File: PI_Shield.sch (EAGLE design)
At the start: 66 parts, among them J10 T2I, J11 T2I, J12 T2I, J13 DF13-4P-1.25DSA, J14 DF13-4P-1.25DSA, J15 DF13-4P-1.25DSA, J16 T2I5P, Q1 220mA/50V/3.5Ω, Q3 220mA/50V/3.5Ω, Q4 220mA/50V/3.5Ω, Q5 2.5A/30V/105mΩ, U1 MAX1136EUA-T, U2 AZ1117EH-3.3TRG1, Y1 ECS-80-S-4X

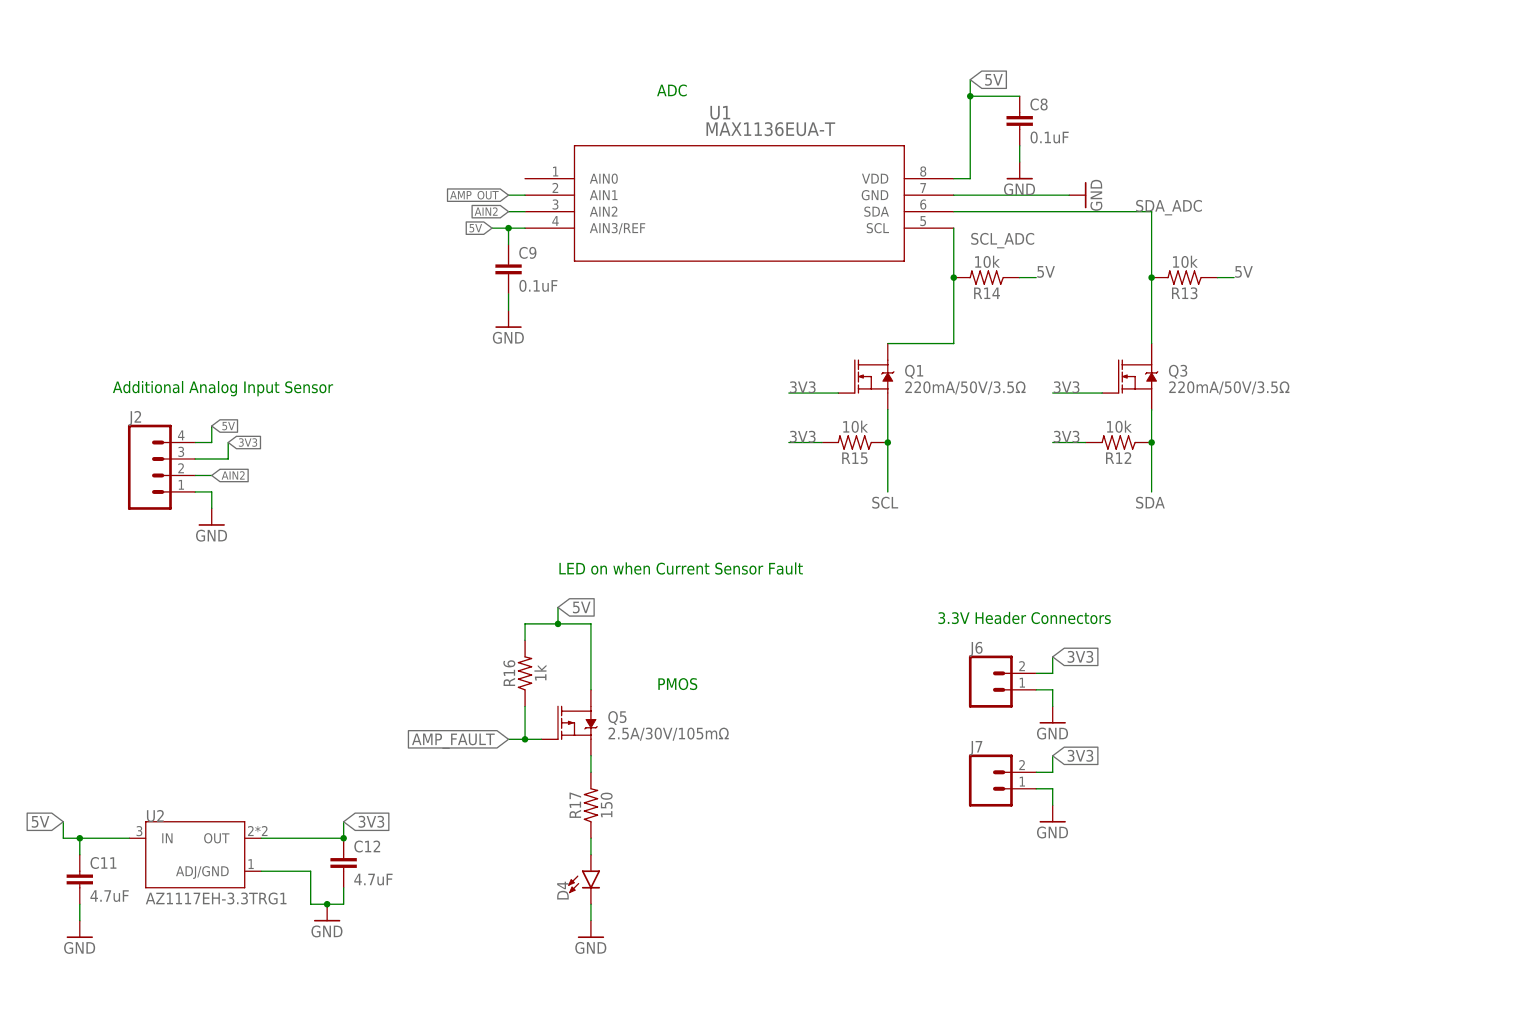
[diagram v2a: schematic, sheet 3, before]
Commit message: Added Pi 4 and Current Sensor; Routed Interrupt pins signals to Pi
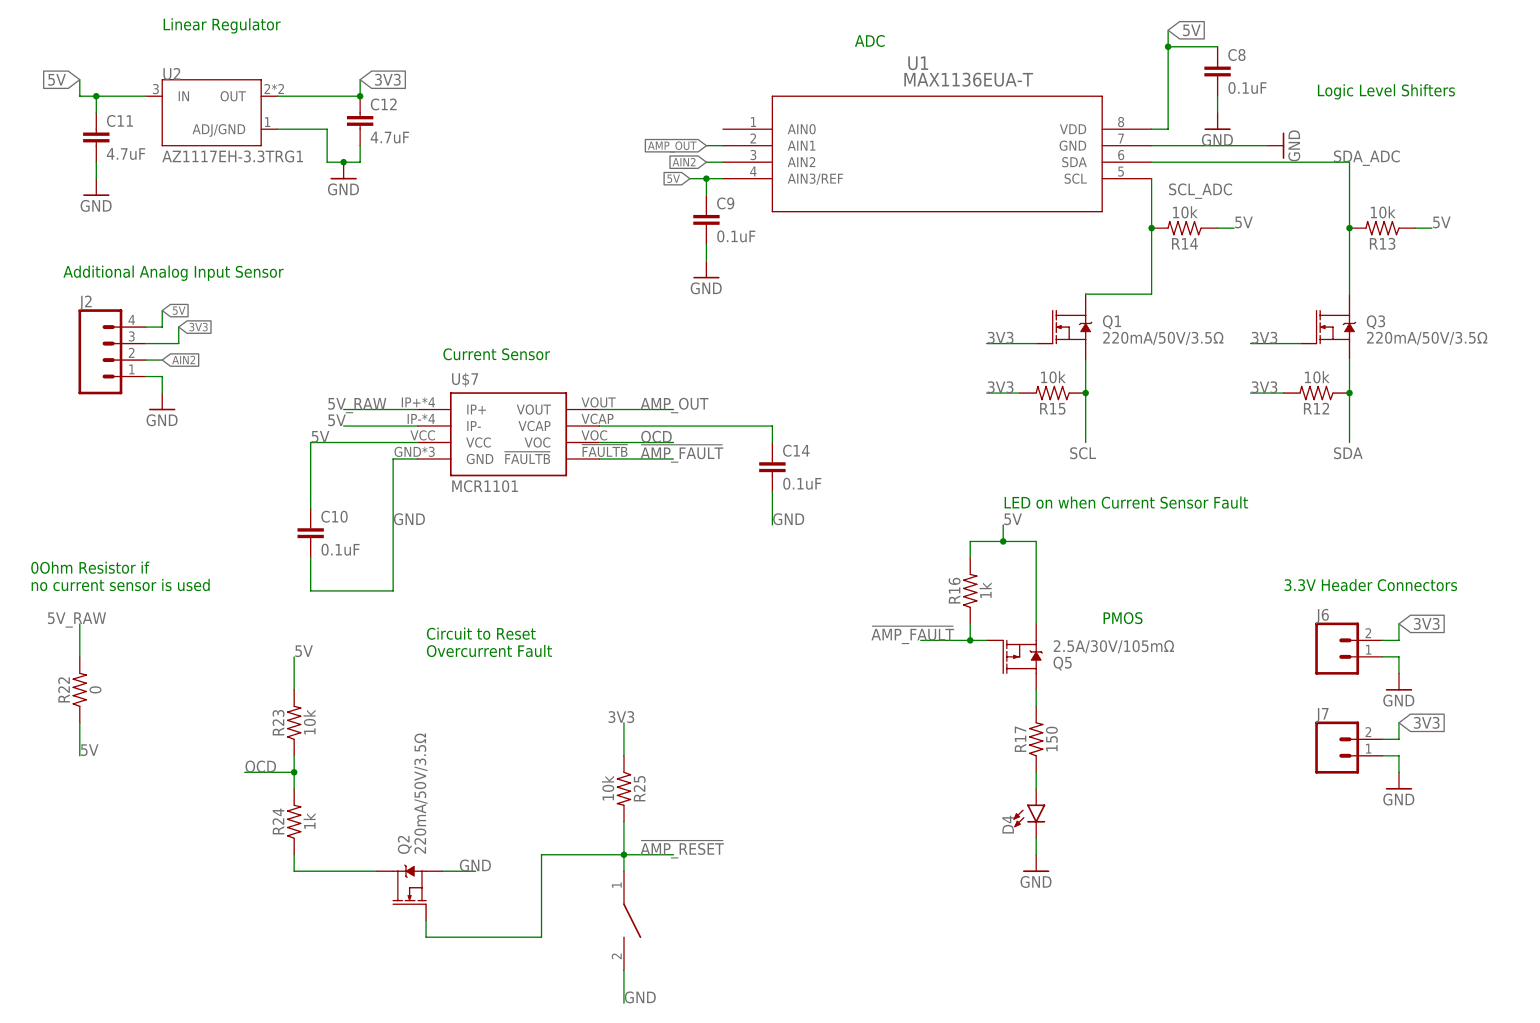
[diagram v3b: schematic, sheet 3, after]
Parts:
- removed PCB1: RPI2, RaspberryPi:RPI2
- added C10, C14: 0.1uF, SparkFun-Capacitors:22NF/22,000PF-0603-50V-10%
- added Q2: 220mA/50V/3.5Ω, SparkFun-DiscreteSemi:MOSFET-NCH-BSS138
- added R22: 0, SparkFun-Resistors:RESISTOR0603
- added R23, R25: 10k, SparkFun-Resistors:RESISTOR0603
- added R24: 1k, SparkFun-Resistors:RESISTOR0603
- added U$7: MCR1101, MCR1101:MCR1101
- added U$8: RPI4, RaspberryPi:RPI4
- U$6: value BNO055_9DOF_BREAKOUT -> (none); device Other:BNO055_9DOF_BREAKOUT -> Push button - FSM2JMTR:DISCRETECOMPONENTS_SWITCH
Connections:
- removed net AMP_FAULT: Q5.G, R16.1
- removed net N$4: U$1.RX0BF
- removed net N$5: U$1.RX1BF
- removed net RESET_TO_PI: PCB1.GPIO22, R10.2
- new net !AMP_FAULT: Q5.G, R16.1, U$7.!FAULTB
- new net !AMP_RESET: Q2.G, R25.2, U$6.P$1, U$8.GPIO4
- new net 5V_RAW: J16.1, J16.2, R22.2, U$3.VCC, U$7.IP+
- new net 9DOF_RST: U$4.RST, U$8.GPIO12
- new net A_INT: U$4.AI1, U$8.GPIO7
- new net CAN_RESET: R10.2, U$8.GPIO22
- new net G_INT: U$4.GI1, U$8.GPIO25
- new net N$13: Q2.D, R24.1
- new net N$6: C14.1, U$7.VCAP
- new net OCD: R23.1, R24.2, U$7.VOC
- new net RX0_INT: U$1.RX0BF, U$8.GPIO26
- new net RX1_INT: U$1.RX1BF, U$8.GPIO5
- net 3V3: now also R25.1
- net 5V: now also C10.1, Q5.S, R22.1, R23.2, U$7.IP-, U$7.VCC; no longer J16.1, J16.2, Q5.D, U$3.VCC
- net AMP_OUT: now also U$7.VOUT
- net CLK: now also U$8.GPIO11; no longer PCB1.GPIO11
- net CS: now also U$8.GPIO8; no longer PCB1.GPIO8
- net DI: now also U$8.GPIO6; no longer PCB1.GPIO6
- net DI1: now also U$8.GPIO16; no longer PCB1.GPIO16
- net DI2: now also U$8.GPIO20; no longer PCB1.GPIO20
- net DI3: now also U$8.GPIO21; no longer PCB1.GPIO21
- net GND: now also C10.2, C14.2, Q2.S, U$6.P$2, U$7.GND, U$8.GND@14, U$8.GND@20, U$8.GND@25, U$8.GND@30, U$8.GND@34, U$8.GND@39, U$8.GND@6, U$8.GND@9; no longer PCB1.GND@14, PCB1.GND@20, PCB1.GND@25, PCB1.GND@30, PCB1.GND@34, PCB1.GND@39, PCB1.GND@6, PCB1.GND@9
- net IMU_INT: now also U$8.GPIO27; no longer PCB1.GPIO27
- net IMU_RESET: now also U$8.GPIO17; no longer PCB1.GPIO17
- net INT: now also U$8.GPIO19; no longer PCB1.GPIO19
- net MISO: now also U$8.GPIO9; no longer PCB1.GPIO9
- net MOSI: now also U$8.GPIO10; no longer PCB1.GPIO10
- net N$10: now also Q5.D; no longer Q5.S
- net PI_POWER: now also U$8.5V@2, U$8.5V@4; no longer PCB1.5V@2, PCB1.5V@4
- net PWM: now also U$8.GPIO13; no longer PCB1.GPIO13
- net RX: now also U$8.GPIO15; no longer PCB1.GPIO15
- net SCL: now also U$8.GPIO3; no longer PCB1.GPIO3
- net SDA: now also U$8.GPIO2; no longer PCB1.GPIO2
- net TX: now also U$8.GPIO14; no longer PCB1.GPIO14
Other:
- note added: "0Ohm Resistor if no current sensor is used"
- note added: "Circuit to Reset Overcurrent Fault"
- note added: "Current Sensor"
- note added: "I2C Pull-up Resistors"
- note added: "Linear Regulator"
- note added: "Logic Level Shifters"
- note removed: "DO NOT USE 27, 28"
- note removed: "DO NOT use pin 28 or 27 these are for EEPROM"
- note removed: "We will be using Pi 4, not Pi 2"
- moved on the sheet: C11, C12, C13, C8, C9, D4, J2, J6, J7, Q1, Q3, Q5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

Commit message: Continuing Layout
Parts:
- C14: value 0.1uF -> .01uF
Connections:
- net CAN_H renamed CAN_P
- net CAN_L renamed CAN_N
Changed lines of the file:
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@@
 <part name="R22" library="SparkFun-Resistors" library_urn="urn:adsk.eagle:library:532" deviceset="RESISTOR" device="0603" package3d_urn="urn:adsk.eagle:package:39650/1" value="0"/>
 <part name="C10" library="SparkFun-Capacitors" library_urn="urn:adsk.eagle:library:510" deviceset="22NF/22,000PF" device="-0603-50V-10%" package3d_urn="urn:adsk.eagle:package:37414/1" value="0.1uF"/>
-<part name="C14" library="SparkFun-Capacitors" library_urn="urn:adsk.eagle:library:510" deviceset="22NF/22,000PF" device="-0603-50V-10%" package3d_urn="urn:adsk.eagle:package:37414/1" value="0.1uF"/>
+<part name="C14" library="SparkFun-Capacitors" library_urn="urn:adsk.eagle:library:510" deviceset="22NF/22,000PF" device="-0603-50V-10%" package3d_urn="urn:adsk.eagle:package:37414/1" value=".01uF"/>
 <part name="R23" library="SparkFun-Resistors" library_urn="urn:adsk.eagle:library:532" deviceset="RESISTOR" device="0603" package3d_urn="urn:adsk.eagle:package:39650/1" value="10k"/>
 <part name="R24" library="SparkFun-Resistors" library_urn="urn:adsk.eagle:library:532" deviceset="RESISTOR" device="0603" package3d_urn="urn:adsk.eagle:package:39650/1" value="1k"/>
@@
 </segment>
 </net>
-<net name="CAN_H" class="1">
+<net name="CAN_P" class="1">
 <segment>
 <pinref part="R6" gate="G$1" pin="2"/>
@@
 </segment>
 </net>
-<net name="CAN_L" class="1">
+<net name="CAN_N" class="1">
 <segment>
 <pinref part="R7" gate="G$1" pin="1"/>
@@
 </segment>
 </net>
-<net name="CAN_H" class="1">
+<net name="CAN_P" class="1">
 <segment>
 <pinref part="J5" gate="G$1" pin="2"/>
@@
 </segment>
 </net>
-<net name="CAN_L" class="1">
+<net name="CAN_N" class="1">
 <segment>
 <pinref part="J5" gate="G$1" pin="1"/>

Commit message: Finished Layout
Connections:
- removed net 9DOF_RST: U$4.RST, U$8.GPIO12
- net IMU_RESET: now also U$4.RST
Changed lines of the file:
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@@
 <label x="58.42" y="43.18" size="1.778" layer="95" xref="yes"/>
+</segment>
+<segment>
+<pinref part="U$4" gate="G$1" pin="RST"/>
+<wire x1="137.16" y1="139.7" x2="129.54" y2="139.7" width="0.1524" layer="91"/>
+<label x="124.46" y="137.16" size="1.778" layer="95"/>
 </segment>
 </net>
@@
 </segment>
 </net>
-<net name="9DOF_RST" class="0">
-<segment>
-<pinref part="U$4" gate="G$1" pin="RST"/>
-<wire x1="137.16" y1="139.7" x2="129.54" y2="139.7" width="0.1524" layer="91"/>
-<label x="124.46" y="137.16" size="1.778" layer="95"/>
-</segment>
-<segment>
-<pinref part="U$8" gate="G$1" pin="GPIO12"/>
-<wire x1="25.4" y1="93.98" x2="20.32" y2="93.98" width="0.1524" layer="91"/>
-<label x="20.32" y="93.98" size="1.778" layer="95" rot="R180" xref="yes"/>
-</segment>
-</net>

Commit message: routed some
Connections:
- net N$9 renamed RESET_MID
- removed net G_INT: U$4.GI1, U$8.GPIO25
- net DI1: now also J12.2; no longer J12.3
- net DI2: now also J12.3; no longer J12.2
- net IMU_INT: now also U$4.GI1
- net INT: now also U$8.GPIO26; no longer U$8.GPIO19
- net RX: now also J8.2; no longer J8.3
- net RX0_INT: now also U$8.GPIO19; no longer U$8.GPIO26
- net TX: now also J8.3; no longer J8.2
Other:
- moved on the sheet: J10, J11, J12
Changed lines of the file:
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@@
 <?xml version="1.0" encoding="utf-8"?>
 <!DOCTYPE eagle SYSTEM "eagle.dtd">
-<eagle version="9.5.2">
+<eagle version="9.6.2">
 <drawing>
 <settings>
@@
 <segment>
 <pinref part="GND11" gate="1" pin="GND"/>
-<wire x1="226.06" y1="43.18" x2="228.6" y2="43.18" width="0.1524" layer="91"/>
+<wire x1="223.52" y1="43.18" x2="228.6" y2="43.18" width="0.1524" layer="91"/>
 <wire x1="228.6" y1="43.18" x2="228.6" y2="40.64" width="0.1524" layer="91"/>
 <pinref part="J12" gate="G$1" pin="4"/>
@@
 </segment>
 <segment>
-<wire x1="238.76" y1="132.08" x2="241.3" y2="132.08" width="0.1524" layer="91"/>
+<wire x1="236.22" y1="132.08" x2="241.3" y2="132.08" width="0.1524" layer="91"/>
 <pinref part="J10" gate="G$1" pin="2"/>
 <label x="241.3" y="132.08" size="1.27" layer="95" xref="yes"/>
 </segment>
 <segment>
-<wire x1="226.06" y1="73.66" x2="228.6" y2="73.66" width="0.1524" layer="91"/>
+<wire x1="223.52" y1="73.66" x2="228.6" y2="73.66" width="0.1524" layer="91"/>
 <pinref part="J11" gate="G$1" pin="2"/>
 <label x="228.6" y="73.66" size="1.27" layer="95" xref="yes"/>
@@
 </segment>
 <segment>
-<wire x1="238.76" y1="129.54" x2="241.3" y2="129.54" width="0.1524" layer="91"/>
+<wire x1="236.22" y1="129.54" x2="241.3" y2="129.54" width="0.1524" layer="91"/>
 <pinref part="J10" gate="G$1" pin="3"/>
 <label x="241.3" y="129.54" size="1.27" layer="95" xref="yes"/>
 </segment>
 <segment>
-<wire x1="226.06" y1="71.12" x2="228.6" y2="71.12" width="0.1524" layer="91"/>
+<wire x1="223.52" y1="71.12" x2="228.6" y2="71.12" width="0.1524" layer="91"/>
 <pinref part="J11" gate="G$1" pin="3"/>
 <label x="228.6" y="71.12" size="1.27" layer="95" xref="yes"/>
@@
 <net name="DI1" class="0">
 <segment>
-<wire x1="226.06" y1="45.72" x2="228.6" y2="45.72" width="0.1524" layer="91"/>
+<wire x1="223.52" y1="48.26" x2="228.6" y2="48.26" width="0.1524" layer="91"/>
+<pinref part="J12" gate="G$1" pin="2"/>
+<label x="228.6" y="48.26" size="1.27" layer="95" xref="yes"/>
+</segment>
+</net>
+<net name="DI2" class="0">
+<segment>
+<wire x1="223.52" y1="45.72" x2="228.6" y2="45.72" width="0.1524" layer="91"/>
 <pinref part="J12" gate="G$1" pin="3"/>
 <label x="228.6" y="45.72" size="1.27" layer="95" xref="yes"/>
-</segment>
-</net>
-<net name="DI2" class="0">
-<segment>
-<wire x1="226.06" y1="48.26" x2="228.6" y2="48.26" width="0.1524" layer="91"/>
-<pinref part="J12" gate="G$1" pin="2"/>
-<label x="228.6" y="48.26" size="1.27" layer="95" xref="yes"/>
 </segment>
 </net>
@@
 </segment>
 </net>
-<net name="N$9" class="0">
+<net name="RESET_MID" class="0">
 <segment>
 <pinref part="R1" gate="G$1" pin="2"/>
@@
 <net name="5V" class="2">
 <segment>
-<wire x1="226.06" y1="50.8" x2="228.6" y2="50.8" width="0.1524" layer="91"/>
+<wire x1="223.52" y1="50.8" x2="228.6" y2="50.8" width="0.1524" layer="91"/>
 <pinref part="J12" gate="G$1" pin="1"/>
 <wire x1="228.6" y1="50.8" x2="228.6" y2="53.34" width="0.1524" layer="91"/>
@@
 <label x="58.42" y="48.26" size="1.778" layer="95" xref="yes"/>
 </segment>
+<segment>
+<pinref part="U$4" gate="G$1" pin="GI1"/>
+<wire x1="167.64" y1="139.7" x2="175.26" y2="139.7" width="0.1524" layer="91"/>
+<label x="172.72" y="139.7" size="1.778" layer="95"/>
+</segment>
 </net>
 <net name="DI" class="0">
@@
 <net name="TX" class="0">
 <segment>
+<pinref part="J8" gate="J$1" pin="3"/>
+<wire x1="142.24" y1="20.32" x2="144.78" y2="20.32" width="0.1524" layer="91"/>
+<label x="144.78" y="20.32" size="1.27" layer="95" xref="yes"/>
+</segment>
+<segment>
+<pinref part="U$8" gate="G$1" pin="GPIO14"/>
+<wire x1="25.4" y1="33.02" x2="20.32" y2="33.02" width="0.1524" layer="91"/>
+<label x="20.32" y="33.02" size="1.778" layer="95" rot="R180" xref="yes"/>
+</segment>
+</net>
+<net name="RX" class="0">
+<segment>
 <pinref part="J8" gate="J$1" pin="2"/>
 <wire x1="142.24" y1="17.78" x2="144.78" y2="17.78" width="0.1524" layer="91"/>
@@
 </segment>
 <segment>
-<pinref part="U$8" gate="G$1" pin="GPIO14"/>
-<wire x1="25.4" y1="33.02" x2="20.32" y2="33.02" width="0.1524" layer="91"/>
-<label x="20.32" y="33.02" size="1.778" layer="95" rot="R180" xref="yes"/>
-</segment>
-</net>
-<net name="RX" class="0">
-<segment>
-<pinref part="J8" gate="J$1" pin="3"/>
-<wire x1="142.24" y1="20.32" x2="144.78" y2="20.32" width="0.1524" layer="91"/>
-<label x="144.78" y="20.32" size="1.27" layer="95" xref="yes"/>
-</segment>
-<segment>
 <pinref part="U$8" gate="G$1" pin="GPIO15"/>
 <wire x1="25.4" y1="38.1" x2="20.32" y2="38.1" width="0.1524" layer="91"/>
@@
 <net name="INT" class="0">
 <segment>
-<pinref part="U$8" gate="G$1" pin="GPIO19"/>
-<wire x1="53.34" y1="104.14" x2="78.74" y2="104.14" width="0.1524" layer="91"/>
-<label x="78.74" y="104.14" size="1.778" layer="95" xref="yes"/>
+<label x="78.74" y="109.22" size="1.778" layer="95" xref="yes"/>
+<pinref part="U$8" gate="G$1" pin="GPIO26"/>
+<wire x1="53.34" y1="109.22" x2="78.74" y2="109.22" width="0.1524" layer="91"/>
 </segment>
 </net>
@@
 </segment>
 </net>
-<net name="G_INT" class="0">
-<segment>
-<pinref part="U$4" gate="G$1" pin="GI1"/>
-<wire x1="167.64" y1="139.7" x2="175.26" y2="139.7" width="0.1524" layer="91"/>
-<label x="172.72" y="139.7" size="1.778" layer="95"/>
-</segment>
-<segment>
-<pinref part="U$8" gate="G$1" pin="GPIO25"/>
-<wire x1="25.4" y1="68.58" x2="20.32" y2="68.58" width="0.1524" layer="91"/>
-<label x="20.32" y="68.58" size="1.778" layer="95" rot="R180" xref="yes"/>
-</segment>
-</net>
 <net name="RX0_INT" class="0">
 <segment>
-<pinref part="U$8" gate="G$1" pin="GPIO26"/>
-<wire x1="53.34" y1="109.22" x2="78.74" y2="109.22" width="0.1524" layer="91"/>
-<label x="78.74" y="109.22" size="1.778" layer="95" xref="yes"/>
-</segment>
-</net>
+<label x="76.2" y="104.14" size="1.778" layer="95" xref="yes"/>
+<pinref part="U$8" gate="G$1" pin="GPIO19"/>
+<wire x1="53.34" y1="104.14" x2="76.2" y2="104.14" width="0.1524" layer="91"/>
+</segment>
+</net>
